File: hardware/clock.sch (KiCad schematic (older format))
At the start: 33 parts, among them SW1 Pulse, SW2 Mode, SW3 Speed, SW4 SW_DIP_x04, U10 74HC14, U11 74HC74, U12 74HC74, U13 74HC253, U14 74HC193, U7 LMC555xN, X1 20MHz

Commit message: Update for ep 11
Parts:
- removed U13: 74HC253, symbol 74xx:74LS253
- added C27, C28: 100n, symbol Device:C_Small
- added U13, U20: 74HC151, symbol 74xx:74LS151
- added U17, U18: 74HC112, symbol 74xx:74LS112
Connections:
- net labels added: RUN
- wire segments 151 -> 216
- no-connect marks 13 -> 15
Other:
- moved on the sheet: C13, C15, C16, C17, C18, C19, C22, C23, C3, R3, R4, RN7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

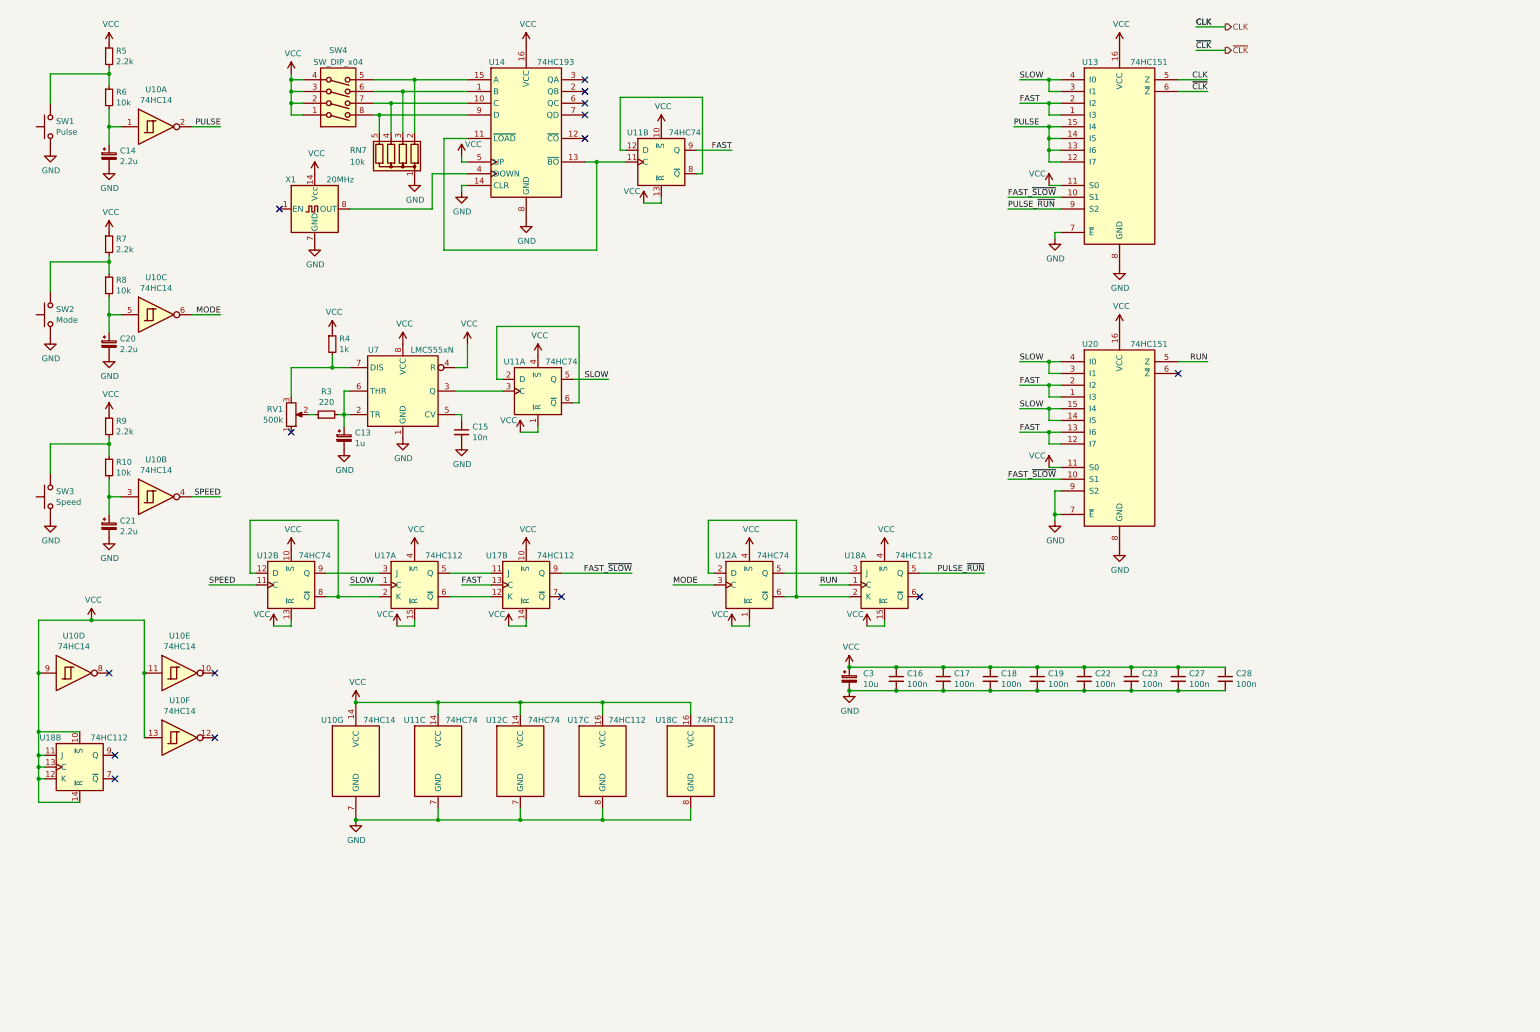
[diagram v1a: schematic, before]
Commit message: Re-number parts
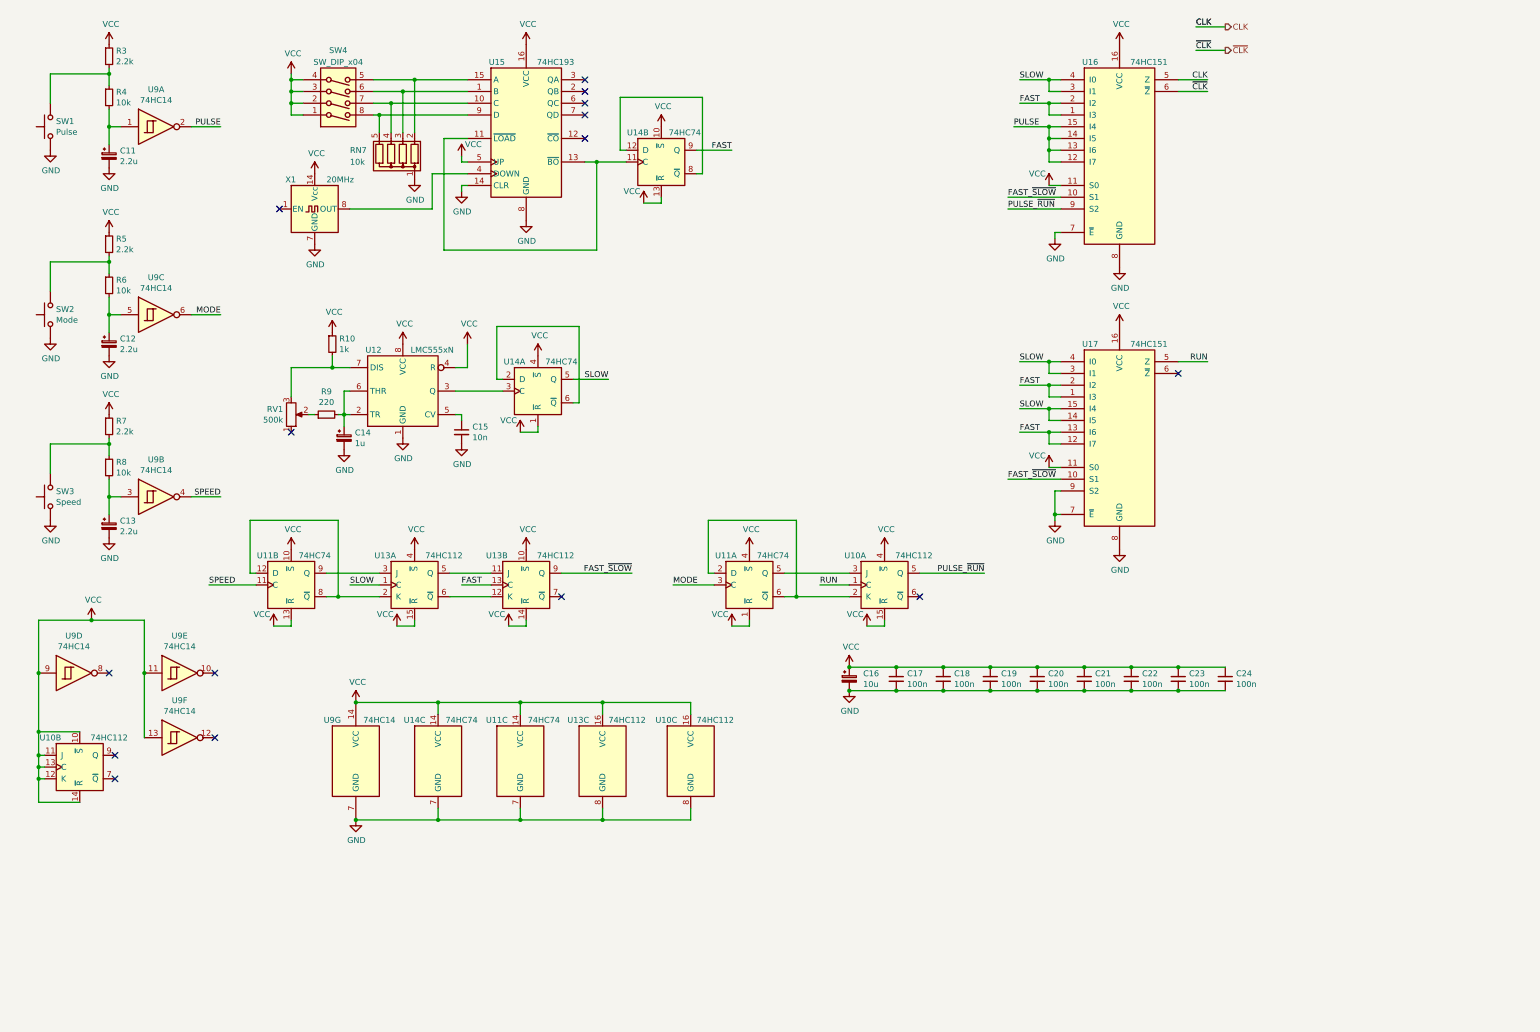
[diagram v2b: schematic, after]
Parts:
- renumbered C14 to C11, C20 to C12, C21 to C13, C13 to C14, C3 to C16, C16 to C17, C17 to C18, C18 to C19, C19 to C20, C22 to C21, C23 to C22, C27 to C23, C28 to C24, R4 to R10, R5 to R3, R6 to R4, R7 to R5, R8 to R6, R9 to R7, R10 to R8, R3 to R9, U18 to U10, U12 to U11, U7 to U12, U17 to U13, U11 to U14, U14 to U15, U13 to U16, U20 to U17, U10 to U9

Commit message: More episode 11 updates
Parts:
- added C29, C30: 100n, symbol Device:C_Small
- added RN8: 10k, Resistor_THT:R_Array_SIP5, symbol Device:R_Network04
- added SW6: SW_DIP_SPDT_x02, symbol 65C816:SW_DIP_SPDT_x02
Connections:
- net GND: now also C29.2, C30.2
- net VCC: now also C29.1, C30.1, RN8.1 (common); no longer U10.15 (~R), U10.4 (~S), U11.1 (~R), U11.10 (~S), U11.13 (~R), U11.4 (~S), U13.10 (~S), U13.14 (~R), U13.15 (~R), U13.4 (~S)
- new net FAST_ON_RST: RN8.2 (R1), SW6.8, U11.10 (~S), U13.10 (~S), U13.4 (~S)
- new net PULSE_ON_RST: RN8.4 (R3), SW6.6, U10.4 (~S), U11.4 (~S)
- new net RUN_ON_RST: RN8.5 (R4), SW6.5, U10.15 (~R), U11.1 (~R)
- new net SLOW_ON_RST: RN8.3 (R2), SW6.7, U11.13 (~R), U13.14 (~R), U13.15 (~R)
- new net ~PWRUP: SW6.1, SW6.2, SW6.3, SW6.4
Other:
- note added: "BOOT SETTING"
- note added: "BUTTONS"
- note added: "FAST CLOCK"
- note added: "MODE SELECT"
- note added: "OUTPUT"
- note added: "RUN CLOCK"
- note added: "SHEET I/O"
- note added: "SLOW CLOCK"
- note added: "SPEED SELECT"
- moved on the sheet: C11, C12, C13, C14, C15, C16, C17, C18, C19, C20, C21, C22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
